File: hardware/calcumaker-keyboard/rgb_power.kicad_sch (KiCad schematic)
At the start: 9 parts, among them Q1 AO3401A, Q2 2N7002, U2 74LVC1G125

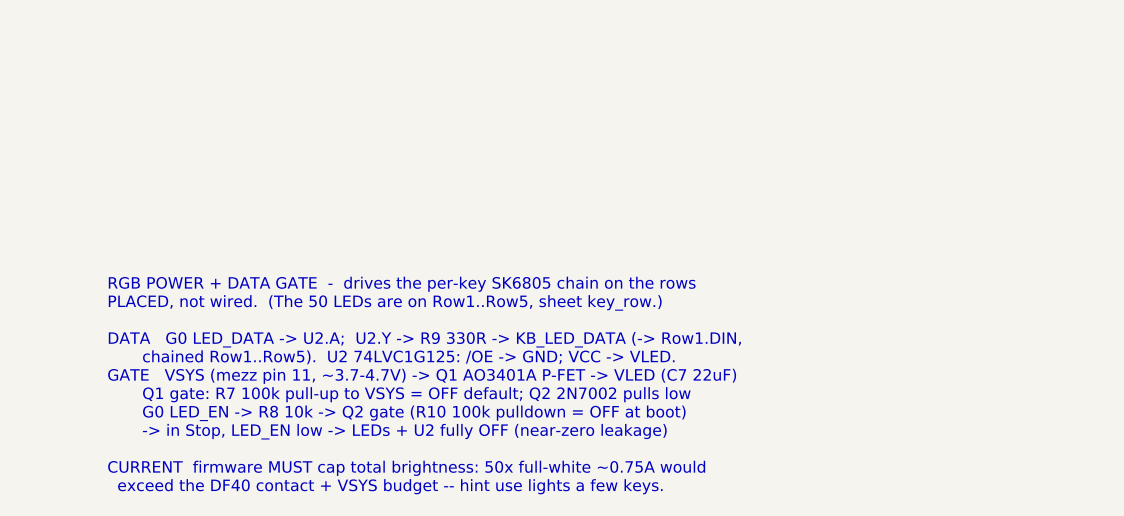
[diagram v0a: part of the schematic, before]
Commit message: hardware: keyswitch 3D models, hot-swap footprint, reverse-mount per-key RGB
Physical build-out of the keyboard: real switch 3D, a hot-swap footprint, and a
single-sided-assembly LED choice.

- 3D models (vendored, hardware/lib/3dmodels): SW_Cherry_MX_1.00u_PCB.step from
  kiswitch/kiswitch (MIT) -- KiCad's Button_Switch_Keyboard.3dshapes does not
  exist in packages3D upstream, so there's nothing to install/download from
  KiCad -- plus HS_CPG151101S11_MX.step (socket) from marbastlib (CERN-OHL-P).
  Also vendor a plain solder-in SW_Cherry_MX_1.00u_PCB.kicad_mod (fallback).

- Keyswitch footprint -> marbastlib SW_MX_HS_CPG151101S11_1u (CERN-OHL-P): the
  Kailh CPG151101S11 hot-swap socket (LCSC C41430893). PLACE-ON-BACK -- switch
  fps go on the board's back copper layer so the socket (authored on F.Cu) lands
  on the physical bottom. HOT-SWAP ONLY: the switch thru-holes are 0.15mm-ring
  socket pass-throughs, NOT solder pads, so a switch-only/solder-in build would
  be a separate board rev (using the vendored solder-in-only fp). The switch-body
  (model) is on the footprint's B side so it renders opposite the socket for
  place-on-back. (Corrects an earlier, wrong "one-board solder+hotswap combo"
  framing -- the pass-throughs don't make a reliable solder joint.)

- Per-key RGB SK6805-EC15 -> SK6812MINI-E (LCSC C5149201), reverse/bottom mount
  (KiCad LED_SK6812MINI-E_3.2x2.8mm_P1.5mm_ReverseMount fp + bundled 3D): the LED
  sits on the bottom with the sockets -> SINGLE-SIDED assembly (one stencil, no
  flip), shining up through the switch's north LED window. Uses the base
  LED:SK6812 symbol (MINI-E `extends` it; kschgen doesn't resolve extends) with
  value/fp/lcsc overridden.

- Docs: DESIGN.md ("Hot-swap switches (place-on-back)" + reverse-mount RGB),
  PARTS.md, both hardware/lib READMEs (with license attribution), memory.

All three boards regenerate + pass the structure check (mcu 55 / keyboard 178 /
display 60, no duplicate refs).

Co-Authored-By: Claude O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
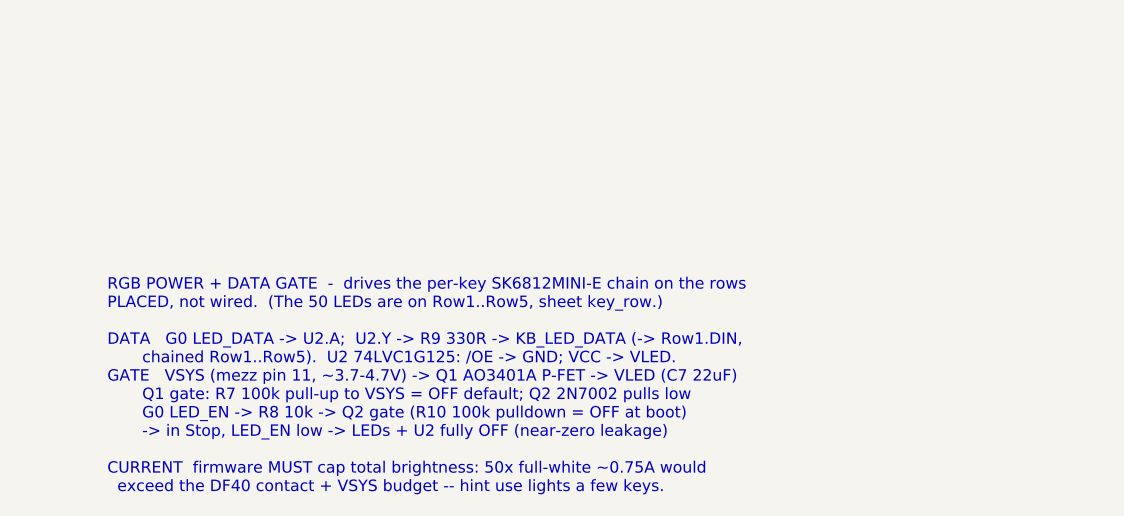
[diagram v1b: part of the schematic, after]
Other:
- note added: "RGB POWER + DATA GATE - drives the per-key SK6812MINI-E chain on the rows PLACED, not wired. (The 50 LEDs are on Row1..Row5, sheet key_row.) DATA G0 LED_DATA -> U2.A; U2.Y -> R9 330R -> KB_LED_DATA (-> Row1.DIN, chained Row1..Row5). U2 74LVC1G125: /OE -> GND; VCC -> VLED. GATE VSYS (mezz pin 11, ~3.7-4.7V) -> Q1 AO3401A P-FET -> VLED (C7 22uF) Q1 gate: R7 100k pull-up to VSYS = OFF default; Q2 2N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"
- note removed: "RGB POWER + DATA GATE - drives the per-key SK6805 chain on the rows PLACED, not wired. (The 50 LEDs are on Row1..Row5, sheet key_row.) DATA G0 LED_DATA -> U2.A; U2.Y -> R9 330R -> KB_LED_DATA (-> Row1.DIN, chained Row1..Row5). U2 74LVC1G125: /OE -> GND; VCC -> VLED. GATE VSYS (mezz pin 11, ~3.7-4.7V) -> Q1 AO3401A P-FET -> VLED (C7 22uF) Q1 gate: R7 100k pull-up to VSYS = OFF default; Q2 2N7002 p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"
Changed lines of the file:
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@@
 		)
 	)
-	(text "RGB POWER + DATA GATE  -  drives the per-key SK6805 chain on the rows\nPLACED, not wired.  (The 50 LEDs are on Row1..Row5, sheet key_row.)\n\nDATA   G0 LED_DATA -> U2.A;  U2.Y -> R9 330R -> KB_LED_DATA (-> Row1.DIN,\n       chained Row1..Row5).  U2 74LVC1G125: /OE -> GND; VCC -> VLED.\nGATE   VSYS (mezz pin 11, ~3.7-4.7V) -> Q1 AO3401A P-FET -> VLED (C7 22uF)\n       Q1 gate: R7 100k pull-up to VSYS = OFF default; Q2 2N7002 pulls low\n       G0 LED_EN -> R8 10k -> Q2 gate (R10 100k pulldown = OFF at boot)\n       -> in Stop, LED_EN low -> LEDs + U2 fully OFF (near-zero leakage)\n\nCURRENT  firmware MUST cap total brightness: 50x full-white ~0.75A would\n  exceed the DF40 contact + VSYS budget -- hint use lights a few keys."
+	(text "RGB POWER + DATA GATE  -  drives the per-key SK6812MINI-E chain on the rows\nPLACED, not wired.  (The 50 LEDs are on Row1..Row5, sheet key_row.)\n\nDATA   G0 LED_DATA -> U2.A;  U2.Y -> R9 330R -> KB_LED_DATA (-> Row1.DIN,\n       chained Row1..Row5).  U2 74LVC1G125: /OE -> GND; VCC -> VLED.\nGATE   VSYS (mezz pin 11, ~3.7-4.7V) -> Q1 AO3401A P-FET -> VLED (C7 22uF)\n       Q1 gate: R7 100k pull-up to VSYS = OFF default; Q2 2N7002 pulls low\n       G0 LED_EN -> R8 10k -> Q2 gate (R10 100k pulldown = OFF at boot)\n       -> in Stop, LED_EN low -> LEDs + U2 fully OFF (near-zero leakage)\n\nCURRENT  firmware MUST cap total brightness: 50x full-white ~0.75A would\n  exceed the DF40 contact + VSYS budget -- hint use lights a few keys."
 		(exclude_from_sim no)
 		(at 15.00 120.00 0)

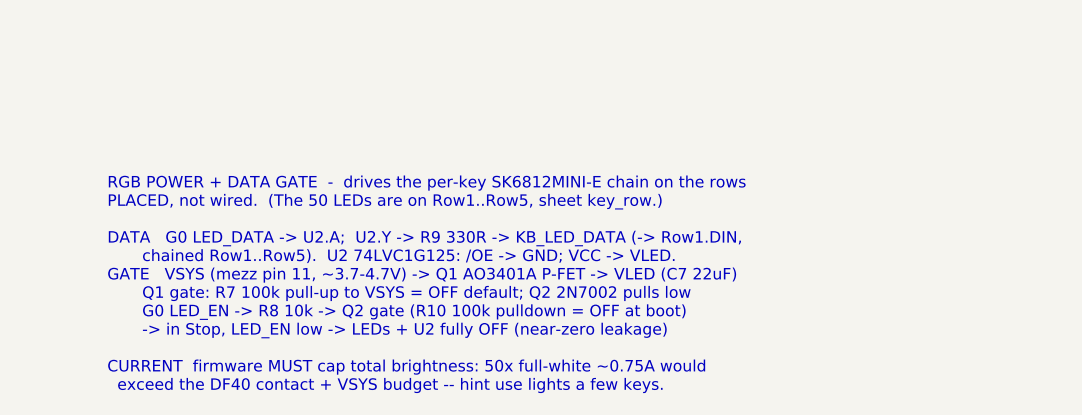
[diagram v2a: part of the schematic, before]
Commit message: hw: regenerate keyboard for the 2U ENTER + vendor the 2U hot-swap footprint
Board files now reflect the 2U ENTER (49 keys):
- key_row.kicad_sch      -> 4 instances (Row1/2/3/5), 30 symbols
- key_row_9.kicad_sch    -> NEW, 1 instance (Row4), 27 symbols: no switch, diode
                            or RGB LED at COL6; refs keep a hole (no SW36/D36/D91)
- root note + rgb_power note updated (49 LEDs, Row4 has 9)

check-calcumaker-keyboard: 176 components (3 fewer), 176/176 footprints assigned,
no duplicate refs, structure sound. Regeneration verified safe first by running the
generator against a scratch copy: the one-off sheets (annunc/kbd_mcu/main_if)
rebuild byte-identical modulo uuids, i.e. nothing was hand-wired.

Vendored calcumaker:SW_MX_HS_CPG151101S11_2u_Vertical -- the 1u hot-swap footprint
plus the four PCB-mount 2U stabilizer NPTH holes (y = +/-11.90mm = 23.8mm spacing;
each wing a 3.05mm hole at x=-7.00 and a 4.00mm at x=+8.24), taken from stock
Button_Switch_Keyboard:SW_Cherry_MX_2.00u_Vertical_PCB and re-expressed about our
origin (already the switch centre). Courtyard grown; 2U keycap envelope on F.Fab.
KiCad 10 parses/plots it (kicad-cli fp export svg).

It is UNUSED by default: we use PLATE-mount stabilizers, which clip into the
switch plate the hot-swap sockets already require, so the PCB needs no stab holes
and ENTER just reuses MX_FP (verified: KiCad's SW_Cherry_MX_2.00u_Vertical_Plate
has the same pad/hole set as the 1u plate fp). PCB-mount would additionally force
a Row5 variant sheet, since ENTER's switch is on the shared 10-key sheet.

Place-on-back is safe: mirroring X maps the stab-hole set onto itself rotated 180,
and a 2U key is symmetric.

Co-Authored-By: Claude Opus 4.8 (1M context) <noreply@anthropic.com>
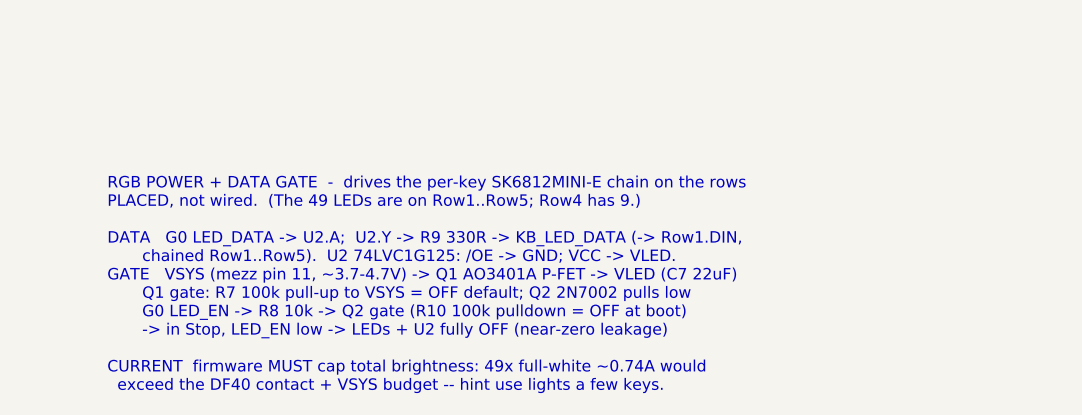
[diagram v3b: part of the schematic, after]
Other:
- note added: "RGB POWER + DATA GATE - drives the per-key SK6812MINI-E chain on the rows PLACED, not wired. (The 49 LEDs are on Row1..Row5; Row4 has 9.) DATA G0 LED_DATA -> U2.A; U2.Y -> R9 330R -> KB_LED_DATA (-> Row1.DIN, chained Row1..Row5). U2 74LVC1G125: /OE -> GND; VCC -> VLED. GATE VSYS (mezz pin 11, ~3.7-4.7V) -> Q1 AO3401A P-FET -> VLED (C7 22uF) Q1 gate: R7 100k pull-up to VSYS = OFF default; Q2 2N700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"
- note removed: "RGB POWER + DATA GATE - drives the per-key SK6812MINI-E chain on the rows PLACED, not wired. (The 50 LEDs are on Row1..Row5, sheet key_row.) DATA G0 LED_DATA -> U2.A; U2.Y -> R9 330R -> KB_LED_DATA (-> Row1.DIN, chained Row1..Row5). U2 74LVC1G125: /OE -> GND; VCC -> VLED. GATE VSYS (mezz pin 11, ~3.7-4.7V) -> Q1 AO3401A P-FET -> VLED (C7 22uF) Q1 gate: R7 100k pull-up to VSYS = OFF default; Q2 2N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"
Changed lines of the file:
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@@
 		)
 	)
-	(text "RGB POWER + DATA GATE  -  drives the per-key SK6812MINI-E chain on the rows\nPLACED, not wired.  (The 50 LEDs are on Row1..Row5, sheet key_row.)\n\nDATA   G0 LED_DATA -> U2.A;  U2.Y -> R9 330R -> KB_LED_DATA (-> Row1.DIN,\n       chained Row1..Row5).  U2 74LVC1G125: /OE -> GND; VCC -> VLED.\nGATE   VSYS (mezz pin 11, ~3.7-4.7V) -> Q1 AO3401A P-FET -> VLED (C7 22uF)\n       Q1 gate: R7 100k pull-up to VSYS = OFF default; Q2 2N7002 pulls low\n       G0 LED_EN -> R8 10k -> Q2 gate (R10 100k pulldown = OFF at boot)\n       -> in Stop, LED_EN low -> LEDs + U2 fully OFF (near-zero leakage)\n\nCURRENT  firmware MUST cap total brightness: 50x full-white ~0.75A would\n  exceed the DF40 contact + VSYS budget -- hint use lights a few keys."
+	(text "RGB POWER + DATA GATE  -  drives the per-key SK6812MINI-E chain on the rows\nPLACED, not wired.  (The 49 LEDs are on Row1..Row5; Row4 has 9.)\n\nDATA   G0 LED_DATA -> U2.A;  U2.Y -> R9 330R -> KB_LED_DATA (-> Row1.DIN,\n       chained Row1..Row5).  U2 74LVC1G125: /OE -> GND; VCC -> VLED.\nGATE   VSYS (mezz pin 11, ~3.7-4.7V) -> Q1 AO3401A P-FET -> VLED (C7 22uF)\n       Q1 gate: R7 100k pull-up to VSYS = OFF default; Q2 2N7002 pulls low\n       G0 LED_EN -> R8 10k -> Q2 gate (R10 100k pulldown = OFF at boot)\n       -> in Stop, LED_EN low -> LEDs + U2 fully OFF (near-zero leakage)\n\nCURRENT  firmware MUST cap total brightness: 49x full-white ~0.74A would\n  exceed the DF40 contact + VSYS budget -- hint use lights a few keys."
 		(exclude_from_sim no)
 		(at 15.00 120.00 0)
